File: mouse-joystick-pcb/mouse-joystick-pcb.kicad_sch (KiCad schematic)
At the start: 0 parts

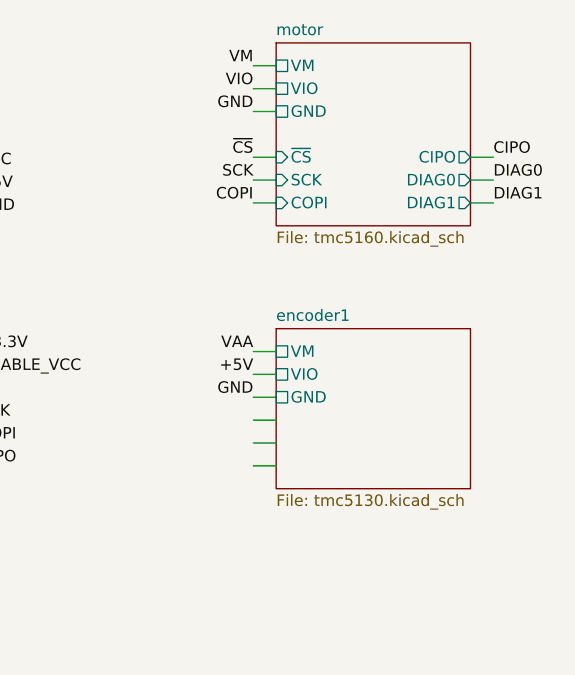
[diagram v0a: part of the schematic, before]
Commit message: Modify schematic for motor-0
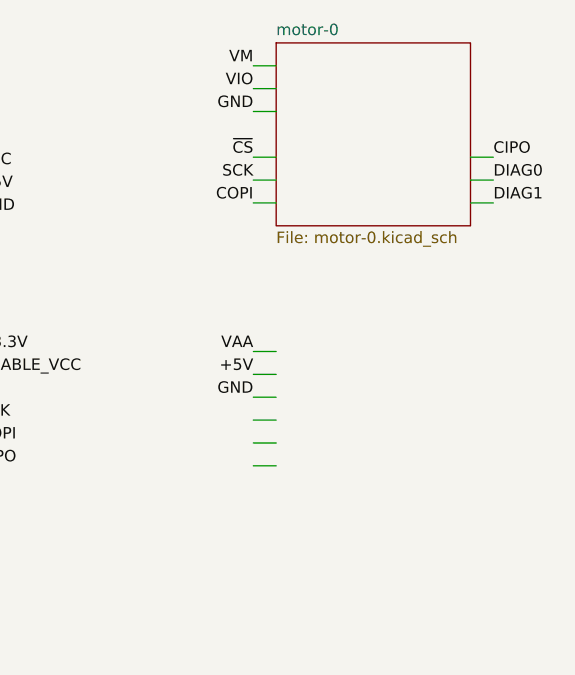
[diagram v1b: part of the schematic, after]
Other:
- removed sheet encoder1
- removed sheet motor
- added sheet motor-0 (motor-0.kicad_sch)
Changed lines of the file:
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@@
   (title_block
     (title "mouse-joystick-pcb")
-    (date "2024-07-27")
+    (date "2024-08-05")
     (rev "1.0")
     (company "Peter Polidoro")
@@
     (stroke (width 0.1524) (type solid))
     (fill (color 0 0 0 0.0000))
-    (property "Sheetname" "motor" (at 129.54 51.3584 0)
+    (property "Sheetname" "motor-0" (at 129.54 51.3584 0)
       (effects (font (size 1.27 1.27)) (justify left bottom))
     )
-    (property "Sheetfile" "tmc5160.kicad_sch" (at 129.54 72.9746 0)
+    (property "Sheetfile" "motor-0.kicad_sch" (at 129.54 72.9746 0)
       (effects (font (size 1.27 1.27)) (justify left top))
-    )
-    (pin "VM" passive (at 129.54 54.61 180)
-      (effects (font (size 1.27 1.27)) (justify left))
-    )
-    (pin "VIO" passive (at 129.54 57.15 180)
-      (effects (font (size 1.27 1.27)) (justify left))
-    )
-    (pin "GND" passive (at 129.54 59.69 180)
-      (effects (font (size 1.27 1.27)) (justify left))
-    )
-    (pin "~{CS}" input (at 129.54 64.77 180)
-      (effects (font (size 1.27 1.27)) (justify left))
-    )
-    (pin "SCK" input (at 129.54 67.31 180)
-      (effects (font (size 1.27 1.27)) (justify left))
-    )
-    (pin "DIAG0" output (at 151.13 67.31 0)
-      (effects (font (size 1.27 1.27)) (justify right))
-    )
-    (pin "DIAG1" output (at 151.13 69.85 0)
-      (effects (font (size 1.27 1.27)) (justify right))
-    )
-    (pin "CIPO" output (at 151.13 64.77 0)
-      (effects (font (size 1.27 1.27)) (justify right))
-    )
-    (pin "COPI" input (at 129.54 69.85 180)
-      (effects (font (size 1.27 1.27)) (justify left))
     )
     (instances
@@
       )
     )
-  )
-  (sheet (at 129.54 83.82) (size 21.59 17.78) (fields_autoplaced)
-    (stroke (width 0.1524) (type solid))
-    (fill (color 0 0 0 0.0000))
-    (property "Sheetname" "encoder1" (at 129.54 83.1084 0)
-      (effects (font (size 1.27 1.27)) (justify left bottom))
-    )
-    (property "Sheetfile" "tmc5130.kicad_sch" (at 129.54 102.1846 0)
-      (effects (font (size 1.27 1.27)) (justify left top))
-    )
-    (pin "VM" passive (at 129.54 86.36 180)
-      (effects (font (size 1.27 1.27)) (justify left))
-    )
-    (pin "VIO" passive (at 129.54 88.9 180)
-      (effects (font (size 1.27 1.27)) (justify left))
-    )
-    (pin "GND" passive (at 129.54 91.44 180)
-      (effects (font (size 1.27 1.27)) (justify left))
-    )
-    (instances
-      (project "mouse-joystick-pcb"
-        (path "/df2b2e89-e055-4140-95de-f1df723db034" (page "14"))
-      )
-    )

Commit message: Add components
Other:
- added sheet audio (audio.kicad_sch)
- sheet microcontroller ports: added none; removed +3.3V, +5V, CIPO, COPI, ENABLE_VCC, GND, SCK
- sheet power ports: added none; removed +5V, ENABLE_VCC, GND, VCC
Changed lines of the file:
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@@
     (company "Peter Polidoro")
-  )
-  (wire (pts (xy 151.13 64.77) (xy 153.67 64.77))
-    (stroke (width 0) (type default))
-  )
-  (wire (pts (xy 151.13 67.31) (xy 153.67 67.31))
-    (stroke (width 0) (type default))
-  )
-  (wire (pts (xy 96.52 68.58) (xy 93.98 68.58))
-    (stroke (width 0) (type default))
-  )
-  (wire (pts (xy 69.85 86.36) (xy 72.39 86.36))
-    (stroke (width 0) (type default))
-  )
-  (wire (pts (xy 96.52 66.04) (xy 93.98 66.04))
-    (stroke (width 0) (type default))
-  )
-  (wire (pts (xy 127 57.15) (xy 129.54 57.15))
-    (stroke (width 0) (type default))
-  )
-  (wire (pts (xy 129.54 69.85) (xy 127 69.85))
-    (stroke (width 0) (type default))
-  )
-  (wire (pts (xy 129.54 99.06) (xy 127 99.06))
-    (stroke (width 0) (type default))
-  )
-  (wire (pts (xy 69.85 88.9) (xy 72.39 88.9))
-    (stroke (width 0) (type default))
-  )
-  (wire (pts (xy 96.52 96.52) (xy 93.98 96.52))
-    (stroke (width 0) (type default))
   )
   (wire (pts (xy 69.85 54.61) (xy 72.39 54.61))
     (stroke (width 0) (type default))
   )
-  (wire (pts (xy 127 88.9) (xy 129.54 88.9))
-    (stroke (width 0) (type default))
-  )
-  (wire (pts (xy 127 91.44) (xy 129.54 91.44))
-    (stroke (width 0) (type default))
-  )
-  (wire (pts (xy 151.13 69.85) (xy 153.67 69.85))
-    (stroke (width 0) (type default))
-  )
-  (wire (pts (xy 96.52 86.36) (xy 93.98 86.36))
-    (stroke (width 0) (type default))
-  )
-  (wire (pts (xy 127 86.36) (xy 129.54 86.36))
-    (stroke (width 0) (type default))
-  )
-  (wire (pts (xy 96.52 99.06) (xy 93.98 99.06))
-    (stroke (width 0) (type default))
-  )
-  (wire (pts (xy 127 59.69) (xy 129.54 59.69))
-    (stroke (width 0) (type default))
-  )
-  (wire (pts (xy 96.52 71.12) (xy 93.98 71.12))
-    (stroke (width 0) (type default))
-  )
-  (wire (pts (xy 129.54 64.77) (xy 127 64.77))
-    (stroke (width 0) (type default))
-  )
-  (wire (pts (xy 93.98 88.9) (xy 96.52 88.9))
-    (stroke (width 0) (type default))
-  )
-  (wire (pts (xy 129.54 93.98) (xy 127 93.98))
-    (stroke (width 0) (type default))
-  )
-  (wire (pts (xy 127 54.61) (xy 129.54 54.61))
-    (stroke (width 0) (type default))
-  )
-  (wire (pts (xy 129.54 96.52) (xy 127 96.52))
-    (stroke (width 0) (type default))
-  )
-  (wire (pts (xy 96.52 93.98) (xy 93.98 93.98))
-    (stroke (width 0) (type default))
-  )
-  (wire (pts (xy 129.54 67.31) (xy 127 67.31))
-    (stroke (width 0) (type default))
-  )
-  (wire (pts (xy 72.39 71.12) (xy 69.85 71.12))
-    (stroke (width 0) (type default))
-  )
-  (label "GND" (at 96.52 71.12 0) (fields_autoplaced)
-    (effects (font (size 1.27 1.27)) (justify left bottom))
-  )
-  (label "COPI" (at 127 69.85 180) (fields_autoplaced)
-    (effects (font (size 1.27 1.27)) (justify right bottom))
-  )
-  (label "SCK" (at 127 67.31 180) (fields_autoplaced)
-    (effects (font (size 1.27 1.27)) (justify right bottom))
-  )
-  (label "VAA" (at 127 86.36 180) (fields_autoplaced)
-    (effects (font (size 1.27 1.27)) (justify right bottom))
-  )
-  (label "COPI" (at 96.52 96.52 0) (fields_autoplaced)
-    (effects (font (size 1.27 1.27)) (justify left bottom))
-  )
-  (label "CIPO" (at 96.52 99.06 0) (fields_autoplaced)
-    (effects (font (size 1.27 1.27)) (justify left bottom))
-  )
-  (label "ENABLE_VCC" (at 96.52 88.9 0) (fields_autoplaced)
-    (effects (font (size 1.27 1.27)) (justify left bottom))
-  )
-  (label "+5V" (at 96.52 68.58 0) (fields_autoplaced)
-    (effects (font (size 1.27 1.27)) (justify left bottom))
-  )
-  (label "~{CS}" (at 127 64.77 180) (fields_autoplaced)
-    (effects (font (size 1.27 1.27)) (justify right bottom))
-  )
-  (label "DIAG0" (at 153.67 67.31 0) (fields_autoplaced)
-    (effects (font (size 1.27 1.27)) (justify left bottom))
-  )
-  (label "SCK" (at 96.52 93.98 0) (fields_autoplaced)
-    (effects (font (size 1.27 1.27)) (justify left bottom))
-  )
-  (label "GND" (at 69.85 88.9 180) (fields_autoplaced)
-    (effects (font (size 1.27 1.27)) (justify right bottom))
-  )
-  (label "VM" (at 127 54.61 180) (fields_autoplaced)
-    (effects (font (size 1.27 1.27)) (justify right bottom))
-  )
-  (label "VIO" (at 127 57.15 180) (fields_autoplaced)
-    (effects (font (size 1.27 1.27)) (justify right bottom))
-  )
-  (label "+5V" (at 127 88.9 180) (fields_autoplaced)
-    (effects (font (size 1.27 1.27)) (justify right bottom))
-  )
-  (label "+5V" (at 69.85 86.36 180) (fields_autoplaced)
-    (effects (font (size 1.27 1.27)) (justify right bottom))
-  )
-  (label "GND" (at 127 59.69 180) (fields_autoplaced)
-    (effects (font (size 1.27 1.27)) (justify right bottom))
-  )
   (label "GND" (at 69.85 54.61 180) (fields_autoplaced)
     (effects (font (size 1.27 1.27)) (justify right bottom))
-  )
-  (label "+3.3V" (at 96.52 86.36 0) (fields_autoplaced)
-    (effects (font (size 1.27 1.27)) (justify left bottom))
-  )
-  (label "GND" (at 127 91.44 180) (fields_autoplaced)
-    (effects (font (size 1.27 1.27)) (justify right bottom))
-  )
-  (label "ENABLE_VCC" (at 69.85 71.12 180) (fields_autoplaced)
-    (effects (font (size 1.27 1.27)) (justify right bottom))
-  )
-  (label "CIPO" (at 153.67 64.77 0) (fields_autoplaced)
-    (effects (font (size 1.27 1.27)) (justify left bottom))
-  )
-  (label "DIAG1" (at 153.67 69.85 0) (fields_autoplaced)
-    (effects (font (size 1.27 1.27)) (justify left bottom))
-  )
-  (label "VCC" (at 96.52 66.04 0) (fields_autoplaced)
-    (effects (font (size 1.27 1.27)) (justify left bottom))
   )
   (sheet (at 72.39 52.07) (size 21.59 5.08) (fields_autoplaced)
@@
       (project "mouse-joystick-pcb"
         (path "/df2b2e89-e055-4140-95de-f1df723db034" (page "2"))
+      )
+    )
+  )
+  (sheet (at 43.18 63.5) (size 15.24 10.16) (fields_autoplaced)
+    (stroke (width 0.1524) (type solid))
+    (fill (color 0 0 0 0.0000))
+    (property "Sheetname" "audio" (at 43.18 62.7884 0)
+      (effects (font (size 1.27 1.27)) (justify left bottom))
+    )
+    (property "Sheetfile" "audio.kicad_sch" (at 43.18 74.2446 0)
+      (effects (font (size 1.27 1.27)) (justify left top))
+    )
+    (instances
+      (project "mouse-joystick-pcb"
+        (path "/df2b2e89-e055-4140-95de-f1df723db034" (page "6"))
       )
     )
@@
       (effects (font (size 1.27 1.27)) (justify left top))
     )
-    (pin "GND" passive (at 72.39 88.9 180)
-      (effects (font (size 1.27 1.27)) (justify left))
-    )
-    (pin "+5V" passive (at 72.39 86.36 180)
-      (effects (font (size 1.27 1.27)) (justify left))
-    )
-    (pin "+3.3V" passive (at 93.98 86.36 0)
-      (effects (font (size 1.27 1.27)) (justify right))
-    )
-    (pin "ENABLE_VCC" output (at 93.98 88.9 0)
-      (effects (font (size 1.27 1.27)) (justify right))
-    )
-    (pin "SCK" output (at 93.98 93.98 0)
-      (effects (font (size 1.27 1.27)) (justify right))
-    )
-    (pin "COPI" output (at 93.98 96.52 0)
-      (effects (font (size 1.27 1.27)) (justify right))
-    )
-    (pin "CIPO" output (at 93.98 99.06 0)
-      (effects (font (size 1.27 1.27)) (justify right))
-    )
     (instances
       (project "mouse-joystick-pcb"
@@
       (effects (font (size 1.27 1.27)) (justify left top))
     )
-    (pin "GND" passive (at 93.98 71.12 0)
-      (effects (font (size 1.27 1.27)) (justify right))
-    )
-    (pin "+5V" passive (at 93.98 68.58 0)
-      (effects (font (size 1.27 1.27)) (justify right))
-    )
-    (pin "ENABLE_VCC" input (at 72.39 71.12 180)
-      (effects (font (size 1.27 1.27)) (justify left))
-    )
-    (pin "VCC" passive (at 93.98 66.04 0)
-      (effects (font (size 1.27 1.27)) (justify right))
-    )
     (instances

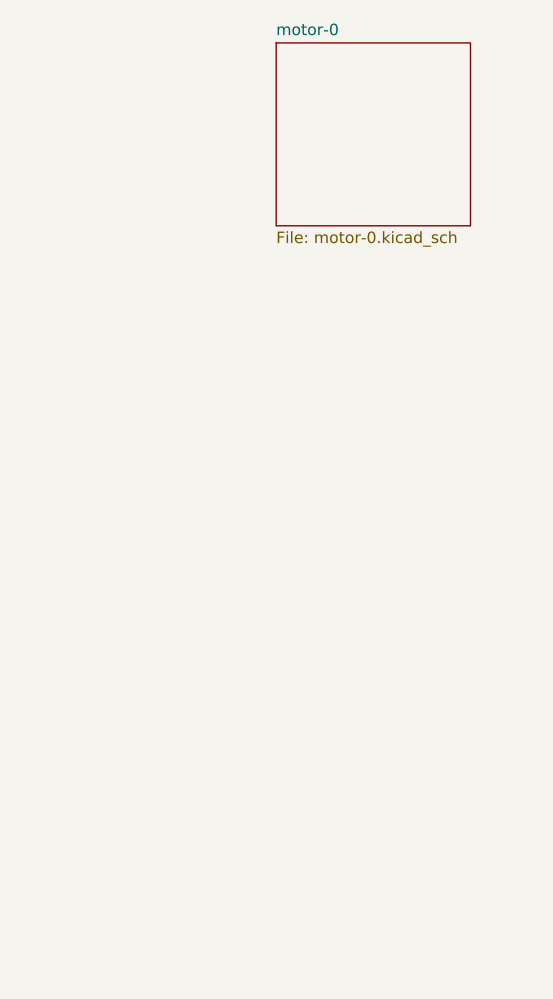
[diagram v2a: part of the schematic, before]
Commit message: Update motor schematics
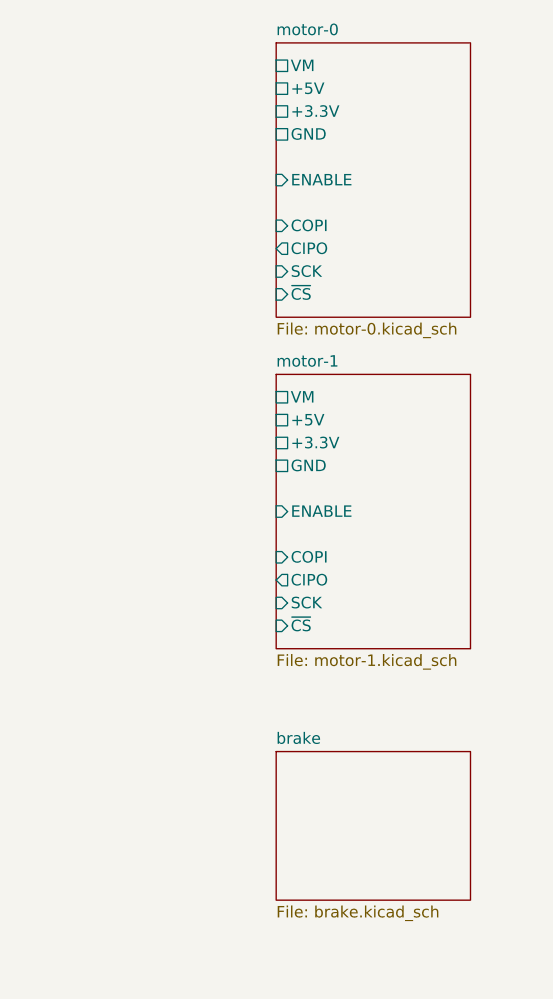
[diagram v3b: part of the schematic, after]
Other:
- added sheet brake (brake.kicad_sch)
- added sheet motor-1 (motor-1.kicad_sch)
- sheet motor-0 ports: added +3.3V, +5V, CIPO, COPI, ENABLE, GND, SCK, VM, ~{CS}; removed none
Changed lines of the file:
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@@
+    )
+  )
+  (sheet (at 129.54 88.9) (size 21.59 30.48) (fields_autoplaced)
+    (stroke (width 0.1524) (type solid))
+    (fill (color 0 0 0 0.0000))
+    (property "Sheetname" "motor-1" (at 129.54 88.1884 0)
+      (effects (font (size 1.27 1.27)) (justify left bottom))
+    )
+    (property "Sheetfile" "motor-1.kicad_sch" (at 129.54 119.9646 0)
+      (effects (font (size 1.27 1.27)) (justify left top))
+    )
+    (pin "GND" passive (at 129.54 99.06 180)
+      (effects (font (size 1.27 1.27)) (justify left))
+    )
+    (pin "VM" passive (at 129.54 91.44 180)
+      (effects (font (size 1.27 1.27)) (justify left))
+    )
+    (pin "+3.3V" passive (at 129.54 96.52 180)
+      (effects (font (size 1.27 1.27)) (justify left))
+    )
+    (pin "+5V" passive (at 129.54 93.98 180)
+      (effects (font (size 1.27 1.27)) (justify left))
+    )
+    (pin "~{CS}" input (at 129.54 116.84 180)
+      (effects (font (size 1.27 1.27)) (justify left))
+    )
+    (pin "SCK" input (at 129.54 114.3 180)
+      (effects (font (size 1.27 1.27)) (justify left))
+    )
+    (pin "ENABLE" input (at 129.54 104.14 180)
+      (effects (font (size 1.27 1.27)) (justify left))
+    )
+    (pin "COPI" input (at 129.54 109.22 180)
+      (effects (font (size 1.27 1.27)) (justify left))
+    )
+    (pin "CIPO" output (at 129.54 111.76 180)
+      (effects (font (size 1.27 1.27)) (justify left))
+    )
+    (instances
+      (project "mouse-joystick-pcb"
+        (path "/df2b2e89-e055-4140-95de-f1df723db034" (page "7"))
+      )
     )
   )
@@
     )
   )
-  (sheet (at 129.54 52.07) (size 21.59 20.32) (fields_autoplaced)
+  (sheet (at 129.54 52.07) (size 21.59 30.48) (fields_autoplaced)
     (stroke (width 0.1524) (type solid))
     (fill (color 0 0 0 0.0000))
@@
       (effects (font (size 1.27 1.27)) (justify left bottom))
     )
-    (property "Sheetfile" "motor-0.kicad_sch" (at 129.54 72.9746 0)
+    (property "Sheetfile" "motor-0.kicad_sch" (at 129.54 83.1346 0)
       (effects (font (size 1.27 1.27)) (justify left top))
+    )
+    (pin "GND" passive (at 129.54 62.23 180)
+      (effects (font (size 1.27 1.27)) (justify left))
+    )
+    (pin "VM" passive (at 129.54 54.61 180)
+      (effects (font (size 1.27 1.27)) (justify left))
+    )
+    (pin "+3.3V" passive (at 129.54 59.69 180)
+      (effects (font (size 1.27 1.27)) (justify left))
+    )
+    (pin "+5V" passive (at 129.54 57.15 180)
+      (effects (font (size 1.27 1.27)) (justify left))
+    )
+    (pin "~{CS}" input (at 129.54 80.01 180)
+      (effects (font (size 1.27 1.27)) (justify left))
+    )
+    (pin "SCK" input (at 129.54 77.47 180)
+      (effects (font (size 1.27 1.27)) (justify left))
+    )
+    (pin "ENABLE" input (at 129.54 67.31 180)
+      (effects (font (size 1.27 1.27)) (justify left))
+    )
+    (pin "COPI" input (at 129.54 72.39 180)
+      (effects (font (size 1.27 1.27)) (justify left))
+    )
+    (pin "CIPO" output (at 129.54 74.93 180)
+      (effects (font (size 1.27 1.27)) (justify left))
     )
     (instances
@@
       )
     )
+  )
+  (sheet (at 129.54 130.81) (size 21.59 16.51) (fields_autoplaced)
+    (stroke (width 0.1524) (type solid))
+    (fill (color 0 0 0 0.0000))
+    (property "Sheetname" "brake" (at 129.54 130.0984 0)
+      (effects (font (size 1.27 1.27)) (justify left bottom))
+    )
+    (property "Sheetfile" "brake.kicad_sch" (at 129.54 147.9046 0)
+      (effects (font (size 1.27 1.27)) (justify left top))
+    )
+    (instances
+      (project "mouse-joystick-pcb"
+        (path "/df2b2e89-e055-4140-95de-f1df723db034" (page "8"))
+      )
+    )

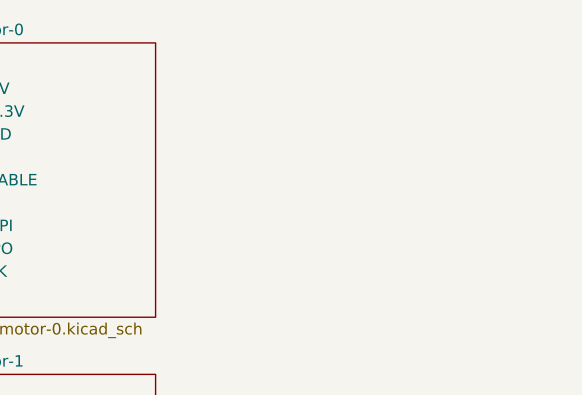
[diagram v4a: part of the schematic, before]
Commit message: Add torque-sensor sheet
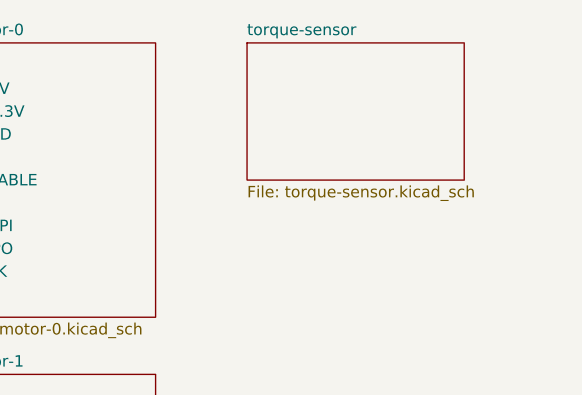
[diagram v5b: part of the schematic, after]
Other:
- added sheet torque-sensor (torque-sensor.kicad_sch)
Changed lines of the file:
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@@
+    )
+  )
+  (sheet (at 161.29 52.07) (size 24.13 15.24) (fields_autoplaced)
+    (stroke (width 0.1524) (type solid))
+    (fill (color 0 0 0 0.0000))
+    (property "Sheetname" "torque-sensor" (at 161.29 51.3584 0)
+      (effects (font (size 1.27 1.27)) (justify left bottom))
+    )
+    (property "Sheetfile" "torque-sensor.kicad_sch" (at 161.29 67.8946 0)
+      (effects (font (size 1.27 1.27)) (justify left top))
+    )
+    (instances
+      (project "mouse-joystick-pcb"
+        (path "/df2b2e89-e055-4140-95de-f1df723db034" (page "9"))
+      )
     )
   )
